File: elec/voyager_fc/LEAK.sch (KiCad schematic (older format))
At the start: 5 parts

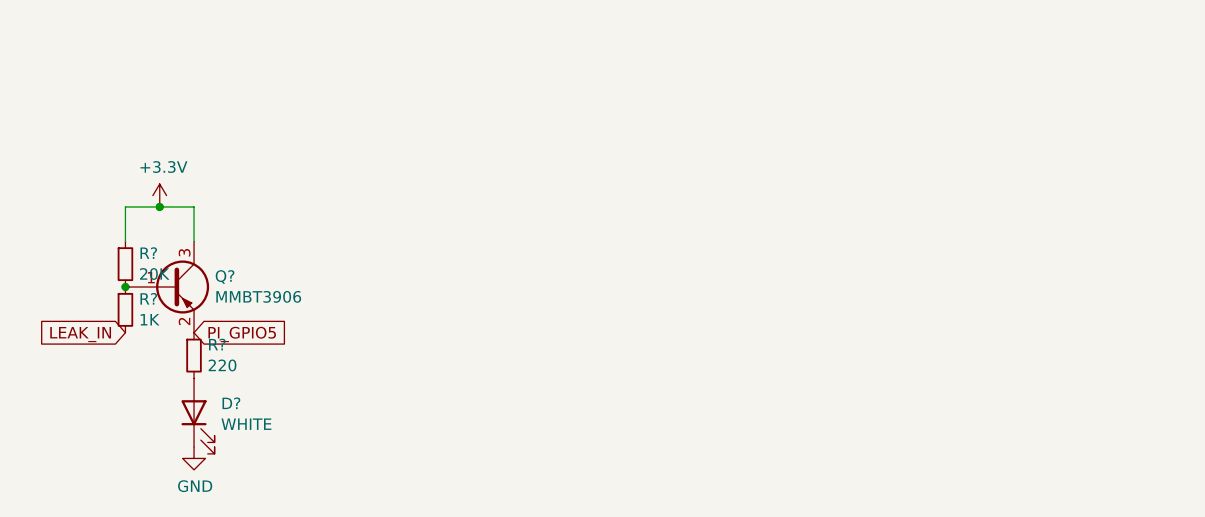
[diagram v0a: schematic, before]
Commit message: Move connectors inside schematics
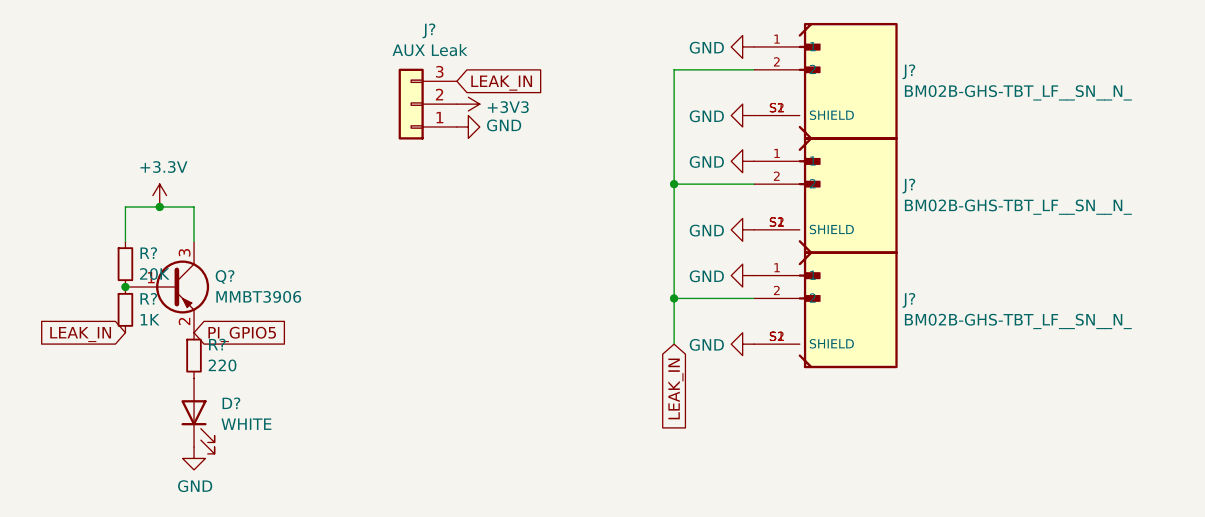
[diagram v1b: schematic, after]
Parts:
- added J? (x3): BM02B-GHS-TBT_LF__SN__N_, JST_BM02B-GHS-TBT_LF__SN__N_, symbol BM02B-GHS-TBT_LF__SN__N_:BM02B-GHS-TBT_LF__SN__N_
- added J?: AUX Leak, Connector_PinHeader_2.54mm:PinHeader_1x03_P2.54mm_Vertical, symbol Connector_Generic:Conn_01x03
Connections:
- net +3V3: now also J?.2 (Pin_2)
- net GND: now also J?.1, J?.1, J?.1, J?.1 (Pin_1), J?.S1 (SHIELD), J?.S1 (SHIELD), J?.S1 (SHIELD), J?.S2 (SHIELD), J?.S2 (SHIELD), J?.S2 (SHIELD)
- net LEAK_IN: now also J?.2, J?.2, J?.2, J?.3 (Pin_3)
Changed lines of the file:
@@
 $Descr A4 11693 8268
 encoding utf-8
-Sheet 6 9
+Sheet 5 9
 Title ""
 Date ""
@@
 U 1 1 67940941
 P 5300 4150
+AR Path="/67940941" Ref="#PWR?"  Part="1"
+AR Path="/6793F336/67940941" Ref="#PWR?"  Part="1"
 F 0 "#PWR?" H 5300 3900 50  0001 C CNN
 F 1 "GND" H 5305 3977 50  0000 C CNN
@@
 U 1 1 6794094C
 P 5150 3100
+AR Path="/6794094C" Ref="#PWR?"  Part="1"
+AR Path="/6793F336/6794094C" Ref="#PWR?"  Part="1"
 F 0 "#PWR?" H 5150 2950 50  0001 C CNN
 F 1 "+3.3V" H 5165 3273 50  0000 C CNN
@@
 U 1 1 67940952
 P 5300 4000
+AR Path="/67940952" Ref="D?"  Part="1"
+AR Path="/6793F336/67940952" Ref="D?"  Part="1"
 F 0 "D?" V 5339 3882 50  0000 R CNN
 F 1 "WHITE" V 5248 3882 50  0000 R CNN
@@
 U 1 1 67940958
 P 5300 3750
+AR Path="/67940958" Ref="R?"  Part="1"
+AR Path="/6793F336/67940958" Ref="R?"  Part="1"
 F 0 "R?" H 5359 3796 50  0000 L CNN
 F 1 "220" H 5359 3705 50  0000 L CNN
@@
 U 1 1 6794095E
 P 5000 3350
+AR Path="/6794095E" Ref="R?"  Part="1"
+AR Path="/6793F336/6794095E" Ref="R?"  Part="1"
 F 0 "R?" H 5059 3396 50  0000 L CNN
 F 1 "20K" H 5059 3305 50  0000 L CNN
@@
 U 1 1 67940965
 P 5000 3550
+AR Path="/67940965" Ref="R?"  Part="1"
+AR Path="/6793F336/67940965" Ref="R?"  Part="1"
 F 0 "R?" H 5059 3596 50  0000 L CNN
 F 1 "1K" H 5059 3505 50  0000 L CNN
@@
 U 1 1 6794096B
 P 5200 3450
+AR Path="/6794096B" Ref="Q?"  Part="1"
+AR Path="/6793F336/6794096B" Ref="Q?"  Part="1"
 F 0 "Q?" H 5391 3496 50  0000 L CNN
 F 1 "MMBT3906" H 5391 3405 50  0000 L CNN
@@
 	1    0    0    -1
 $EndComp
+$Comp
+L BM02B-GHS-TBT_LF__SN__N_:BM02B-GHS-TBT_LF__SN__N_ J?
+U 1 1 67D90B0B
+P 8150 3500
+F 0 "J?" H 8403 3496 50  0000 L CNN
+F 1 "BM02B-GHS-TBT_LF__SN__N_" H 8403 3405 50  0000 L CNN
+F 2 "JST_BM02B-GHS-TBT_LF__SN__N_" H 8150 3500 50  0001 L BNN
+F 3 "" H 8150 3500 50  0001 L BNN
+F 4 "JST Sales" H 8150 3500 50  0001 L BNN "MF"
+F 5 "4.05 mm" H 8150 3500 50  0001 L BNN "MAXIMUM_PACKAGE_HEIGHT"
+F 6 "None" H 8150 3500 50  0001 L BNN "Package"
+F 7 "None" H 8150 3500 50  0001 L BNN "Price"
+F 8 "https://www.snapeda.com/parts/BM02B-GHS-TBT(LF)(SN)(N)/JST+Sales+America+Inc./view-part/?ref=eda" H 8150 3500 50  0001 L BNN "Check_prices"
+F 9 "Manufacturer Recommendations" H 8150 3500 50  0001 L BNN "STANDARD"
+F 10 "https://www.snapeda.com/parts/BM02B-GHS-TBT(LF)(SN)(N)/JST+Sales+America+Inc./view-part/?ref=snap" H 8150 3500 50  0001 L BNN "SnapEDA_Link"
+F 11 "BM02B-GHS-TBT(LF)(SN)(N)" H 8150 3500 50  0001 L BNN "MP"
+F 12 "\\n                        \\n                            Connector Header Surface Mount 2 position 0.049 (1.25mm)\\n                        \\n" H 8150 3500 50  0001 L BNN "Description"
+F 13 "In Stock" H 8150 3500 50  0001 L BNN "Availability"
+F 14 "JST" H 8150 3500 50  0001 L BNN "MANUFACTURER"
+	1    8150 3500
+	1    0    0    -1
+$EndComp
+$Comp
+L BM02B-GHS-TBT_LF__SN__N_:BM02B-GHS-TBT_LF__SN__N_ J?
+U 1 1 67D90B1C
+P 8150 3000
+F 0 "J?" H 8403 2996 50  0000 L CNN
+F 1 "BM02B-GHS-TBT_LF__SN__N_" H 8403 2905 50  0000 L CNN
+F 2 "JST_BM02B-GHS-TBT_LF__SN__N_" H 8150 3000 50  0001 L BNN
+F 3 "" H 8150 3000 50  0001 L BNN
+F 4 "JST Sales" H 8150 3000 50  0001 L BNN "MF"
+F 5 "4.05 mm" H 8150 3000 50  0001 L BNN "MAXIMUM_PACKAGE_HEIGHT"
+F 6 "None" H 8150 3000 50  0001 L BNN "Package"
+F 7 "None" H 8150 3000 50  0001 L BNN "Price"
+F 8 "https://www.snapeda.com/parts/BM02B-GHS-TBT(LF)(SN)(N)/JST+Sales+America+Inc./view-part/?ref=eda" H 8150 3000 50  0001 L BNN "Check_prices"
+F 9 "Manufacturer Recommendations" H 8150 3000 50  0001 L BNN "STANDARD"
+F 10 "https://www.snapeda.com/parts/BM02B-GHS-TBT(LF)(SN)(N)/JST+Sales+America+Inc./view-part/?ref=snap" H 8150 3000 50  0001 L BNN "SnapEDA_Link"
+F 11 "BM02B-GHS-TBT(LF)(SN)(N)" H 8150 3000 50  0001 L BNN "MP"
+F 12 "\\n                        \\n                            Connector Header Surface Mount 2 position 0.049 (1.25mm)\\n                        \\n" H 8150 3000 50  0001 L BNN "Description"
+F 13 "In Stock" H 8150 3000 50  0001 L BNN "Availability"
+F 14 "JST" H 8150 3000 50  0001 L BNN "MANUFACTURER"
+	1    8150 3000
+	1    0    0    -1
+$EndComp
+$Comp
+L BM02B-GHS-TBT_LF__SN__N_:BM02B-GHS-TBT_LF__SN__N_ J?
+U 1 1 67D90B2D
+P 8150 2500
+F 0 "J?" H 8403 2496 50  0000 L CNN
+F 1 "BM02B-GHS-TBT_LF__SN__N_" H 8403 2405 50  0000 L CNN
+F 2 "JST_BM02B-GHS-TBT_LF__SN__N_" H 8150 2500 50  0001 L BNN
+F 3 "" H 8150 2500 50  0001 L BNN
+F 4 "JST Sales" H 8150 2500 50  0001 L BNN "MF"
+F 5 "4.05 mm" H 8150 2500 50  0001 L BNN "MAXIMUM_PACKAGE_HEIGHT"
+F 6 "None" H 8150 2500 50  0001 L BNN "Package"
+F 7 "None" H 8150 2500 50  0001 L BNN "Price"
+F 8 "https://www.snapeda.com/parts/BM02B-GHS-TBT(LF)(SN)(N)/JST+Sales+America+Inc./view-part/?ref=eda" H 8150 2500 50  0001 L BNN "Check_prices"
+F 9 "Manufacturer Recommendations" H 8150 2500 50  0001 L BNN "STANDARD"
+F 10 "https://www.snapeda.com/parts/BM02B-GHS-TBT(LF)(SN)(N)/JST+Sales+America+Inc./view-part/?ref=snap" H 8150 2500 50  0001 L BNN "SnapEDA_Link"
+F 11 "BM02B-GHS-TBT(LF)(SN)(N)" H 8150 2500 50  0001 L BNN "MP"
+F 12 "\\n                        \\n                            Connector Header Surface Mount 2 position 0.049 (1.25mm)\\n                        \\n" H 8150 2500 50  0001 L BNN "Description"
+F 13 "In Stock" H 8150 2500 50  0001 L BNN "Availability"
+F 14 "JST" H 8150 2500 50  0001 L BNN "MANUFACTURER"
+	1    8150 2500
+	1    0    0    -1
+$EndComp
+Wire Wire Line
+	7400 3000 7400 3500
+Connection ~ 7400 3000
+Wire Wire Line
+	7400 3500 7400 3700
+Connection ~ 7400 3500
+Wire Wire Line
+	7400 2500 7400 3000
+Wire Wire Line
+	7750 3500 7400 3500
+Wire Wire Line
+	7750 3000 7400 3000
+Wire Wire Line
+	7750 2500 7400 2500
+$Comp
+L power:GND #PWR?
+U 1 1 67D90B3B
+P 7750 2900
+F 0 "#PWR?" H 7750 2650 50  0001 C CNN
+F 1 "GND" V 7755 2772 50  0000 R CNN
+F 2 "" H 7750 2900 50  0001 C CNN
+F 3 "" H 7750 2900 50  0001 C CNN
+	1    7750 2900
+	0    1    1    0
+$EndComp
+$Comp
+L power:GND #PWR?
+U 1 1 67D90B41
+P 7750 2700
+F 0 "#PWR?" H 7750 2450 50  0001 C CNN
+F 1 "GND" V 7755 2572 50  0000 R CNN
+F 2 "" H 7750 2700 50  0001 C CNN
+F 3 "" H 7750 2700 50  0001 C CNN
+	1    7750 2700
+	0    1    1    0
+$EndComp
+$Comp
+L power:GND #PWR?
+U 1 1 67D90B47
+P 7750 3700
+F 0 "#PWR?" H 7750 3450 50  0001 C CNN
+F 1 "GND" V 7755 3572 50  0000 R CNN
+F 2 "" H 7750 3700 50  0001 C CNN
+F 3 "" H 7750 3700 50  0001 C CNN
+	1    7750 3700
+	0    1    1    0
+$EndComp
+$Comp
+L power:GND #PWR?
+U 1 1 67D90B4D
+P 7750 3400
+F 0 "#PWR?" H 7750 3150 50  0001 C CNN
+F 1 "GND" V 7755 3272 50  0000 R CNN
+F 2 "" H 7750 3400 50  0001 C CNN
+F 3 "" H 7750 3400 50  0001 C CNN
+	1    7750 3400
+	0    1    1    0
+$EndComp
+$Comp
+L power:GND #PWR?
+U 1 1 67D90B53
+P 7750 3200
+F 0 "#PWR?" H 7750 2950 50  0001 C CNN
+F 1 "GND" V 7755 3072 50  0000 R CNN
+F 2 "" H 7750 3200 50  0001 C CNN
+F 3 "" H 7750 3200 50  0001 C CNN
+	1    7750 3200
+	0    1    1    0
+$EndComp
+$Comp
+L power:GND #PWR?
+U 1 1 67D90B59
+P 7750 2400
+F 0 "#PWR?" H 7750 2150 50  0001 C CNN
+F 1 "GND" V 7755 2272 50  0000 R CNN
+F 2 "" H 7750 2400 50  0001 C CNN
+F 3 "" H 7750 2400 50  0001 C CNN
+	1    7750 2400
+	0    1    1    0
+$EndComp
+Text GLabel 7400 3700 3    50   Input ~ 0
+LEAK_IN
+$Comp
+L power:GND #PWR?
+U 1 1 67D90B60
+P 6450 2750
+F 0 "#PWR?" H 6450 2500 50  0001 C CNN
+F 1 "GND" V 6455 2622 50  0000 R CNN
+F 2 "" H 6450 2750 50  0001 C CNN
+F 3 "" H 6450 2750 50  0001 C CNN
+	1    6450 2750
+	0    -1   -1   0
+$EndComp
+Text GLabel 6450 2550 2    50   Input ~ 0
+LEAK_IN
+$Comp
+L power:+3V3 #PWR?
+U 1 1 67D90B67
+P 6450 2650
+F 0 "#PWR?" H 6450 2500 50  0001 C CNN
+F 1 "+3V3" V 6465 2778 50  0000 L CNN
+F 2 "" H 6450 2650 50  0001 C CNN
+F 3 "" H 6450 2650 50  0001 C CNN
+	1    6450 2650
+	0    1    1    0
+$EndComp
+$Comp
+L Connector_Generic:Conn_01x03 J?
+U 1 1 67D90B6D
+P 6250 2650
+F 0 "J?" H 6168 2325 50  0000 C CNN
+F 1 "AUX Leak" H 6168 2416 50  0000 C CNN
+F 2 "Connector_PinHeader_2.54mm:PinHeader_1x03_P2.54mm_Vertical" H 6250 2650 50  0001 C CNN
+F 3 "~" H 6250 2650 50  0001 C CNN
+	1    6250 2650
+	-1   0    0    1
+$EndComp
 $EndSCHEMATC

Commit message: Place all components and start route
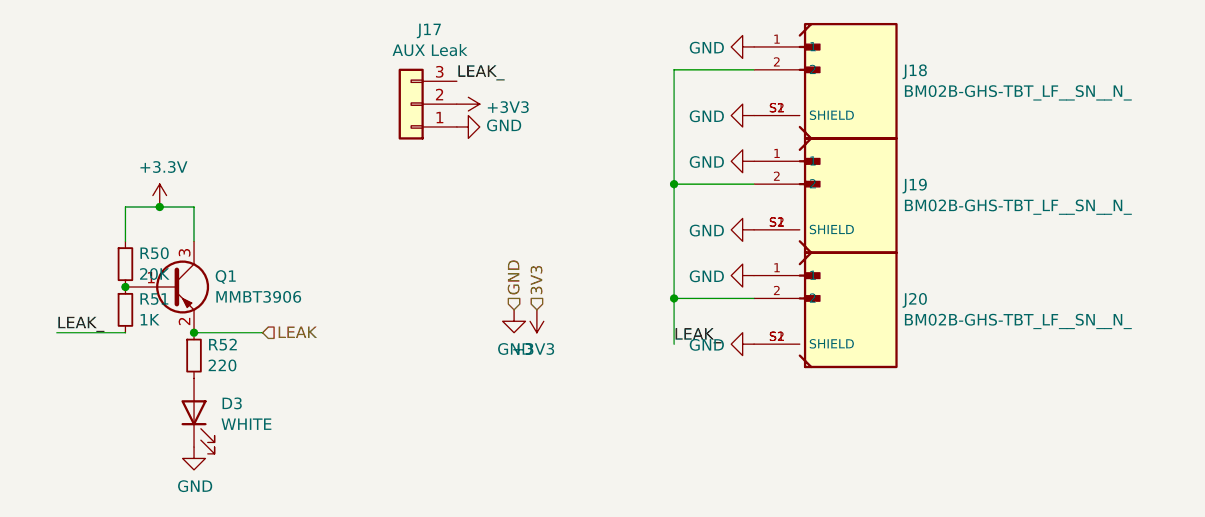
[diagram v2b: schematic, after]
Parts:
- J18, J19, J20: renamed from J?; footprint JST_BM02B-GHS-TBT_LF__SN__N_ -> BM02B-GHS-TBT_LF__SN__N_:JST_BM02B-GHS-TBT_LF__SN__N_
- R52: renamed from R?; footprint Resistor_SMD:R_0603_1608Metric -> Resistor_SMD:R_0402_1005Metric
- gave numbers to parts that had none: 5
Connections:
- net LEAK_IN renamed LEAK_
- net PI_GPIO5 renamed LEAK
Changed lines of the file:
@@
 $Descr A4 11693 8268
 encoding utf-8
-Sheet 5 9
+Sheet 5 10
 Title ""
 Date ""
@@
 Comment4 ""
 $EndDescr
-Text GLabel 5300 3650 2    50   Input ~ 0
-PI_GPIO5
-Text GLabel 5000 3650 0    50   Input ~ 0
-LEAK_IN
 $Comp
 L power:GND #PWR?
@@
 P 5300 4150
 AR Path="/67940941" Ref="#PWR?"  Part="1"
-AR Path="/6793F336/67940941" Ref="#PWR?"  Part="1"
-F 0 "#PWR?" H 5300 3900 50  0001 C CNN
+AR Path="/6793F336/67940941" Ref="#PWR0130"  Part="1"
+F 0 "#PWR0130" H 5300 3900 50  0001 C CNN
 F 1 "GND" H 5305 3977 50  0000 C CNN
 F 2 "" H 5300 4150 50  0001 C CNN
@@
 P 5150 3100
 AR Path="/6794094C" Ref="#PWR?"  Part="1"
-AR Path="/6793F336/6794094C" Ref="#PWR?"  Part="1"
-F 0 "#PWR?" H 5150 2950 50  0001 C CNN
+AR Path="/6793F336/6794094C" Ref="#PWR0129"  Part="1"
+F 0 "#PWR0129" H 5150 2950 50  0001 C CNN
 F 1 "+3.3V" H 5165 3273 50  0000 C CNN
 F 2 "" H 5150 3100 50  0001 C CNN
@@
 P 5300 4000
 AR Path="/67940952" Ref="D?"  Part="1"
-AR Path="/6793F336/67940952" Ref="D?"  Part="1"
-F 0 "D?" V 5339 3882 50  0000 R CNN
+AR Path="/6793F336/67940952" Ref="D3"  Part="1"
+F 0 "D3" V 5339 3882 50  0000 R CNN
 F 1 "WHITE" V 5248 3882 50  0000 R CNN
 F 2 "LED_SMD:LED_0603_1608Metric" H 5300 4000 50  0001 C CNN
@@
 P 5300 3750
 AR Path="/67940958" Ref="R?"  Part="1"
-AR Path="/6793F336/67940958" Ref="R?"  Part="1"
-F 0 "R?" H 5359 3796 50  0000 L CNN
+AR Path="/6793F336/67940958" Ref="R52"  Part="1"
+F 0 "R52" H 5359 3796 50  0000 L CNN
 F 1 "220" H 5359 3705 50  0000 L CNN
-F 2 "Resistor_SMD:R_0603_1608Metric" H 5300 3750 50  0001 C CNN
+F 2 "Resistor_SMD:R_0402_1005Metric" H 5300 3750 50  0001 C CNN
 F 3 "~" H 5300 3750 50  0001 C CNN
 	1    5300 3750
@@
 P 5000 3350
 AR Path="/6794095E" Ref="R?"  Part="1"
-AR Path="/6793F336/6794095E" Ref="R?"  Part="1"
-F 0 "R?" H 5059 3396 50  0000 L CNN
+AR Path="/6793F336/6794095E" Ref="R50"  Part="1"
+F 0 "R50" H 5059 3396 50  0000 L CNN
 F 1 "20K" H 5059 3305 50  0000 L CNN
 F 2 "Resistor_SMD:R_0603_1608Metric" H 5000 3350 50  0001 C CNN
@@
 P 5000 3550
 AR Path="/67940965" Ref="R?"  Part="1"
-AR Path="/6793F336/67940965" Ref="R?"  Part="1"
-F 0 "R?" H 5059 3596 50  0000 L CNN
+AR Path="/6793F336/67940965" Ref="R51"  Part="1"
+F 0 "R51" H 5059 3596 50  0000 L CNN
 F 1 "1K" H 5059 3505 50  0000 L CNN
 F 2 "Resistor_SMD:R_0603_1608Metric" H 5000 3550 50  0001 C CNN
@@
 P 5200 3450
 AR Path="/6794096B" Ref="Q?"  Part="1"
-AR Path="/6793F336/6794096B" Ref="Q?"  Part="1"
-F 0 "Q?" H 5391 3496 50  0000 L CNN
+AR Path="/6793F336/6794096B" Ref="Q1"  Part="1"
+F 0 "Q1" H 5391 3496 50  0000 L CNN
 F 1 "MMBT3906" H 5391 3405 50  0000 L CNN
 F 2 "Package_TO_SOT_SMD:SOT-23" H 5400 3375 50  0001 L CIN
@@
 U 1 1 67D90B0B
 P 8150 3500
-F 0 "J?" H 8403 3496 50  0000 L CNN
+AR Path="/67D90B0B" Ref="J?"  Part="1"
+AR Path="/6793F336/67D90B0B" Ref="J20"  Part="1"
+F 0 "J20" H 8403 3496 50  0000 L CNN
 F 1 "BM02B-GHS-TBT_LF__SN__N_" H 8403 3405 50  0000 L CNN
-F 2 "JST_BM02B-GHS-TBT_LF__SN__N_" H 8150 3500 50  0001 L BNN
+F 2 "BM02B-GHS-TBT_LF__SN__N_:JST_BM02B-GHS-TBT_LF__SN__N_" H 8150 3500 50  0001 L BNN
 F 3 "" H 8150 3500 50  0001 L BNN
 F 4 "JST Sales" H 8150 3500 50  0001 L BNN "MF"
@@
 U 1 1 67D90B1C
 P 8150 3000
-F 0 "J?" H 8403 2996 50  0000 L CNN
+AR Path="/67D90B1C" Ref="J?"  Part="1"
+AR Path="/6793F336/67D90B1C" Ref="J19"  Part="1"
+F 0 "J19" H 8403 2996 50  0000 L CNN
 F 1 "BM02B-GHS-TBT_LF__SN__N_" H 8403 2905 50  0000 L CNN
-F 2 "JST_BM02B-GHS-TBT_LF__SN__N_" H 8150 3000 50  0001 L BNN
+F 2 "BM02B-GHS-TBT_LF__SN__N_:JST_BM02B-GHS-TBT_LF__SN__N_" H 8150 3000 50  0001 L BNN
 F 3 "" H 8150 3000 50  0001 L BNN
 F 4 "JST Sales" H 8150 3000 50  0001 L BNN "MF"
@@
 U 1 1 67D90B2D
 P 8150 2500
-F 0 "J?" H 8403 2496 50  0000 L CNN
+AR Path="/67D90B2D" Ref="J?"  Part="1"
+AR Path="/6793F336/67D90B2D" Ref="J18"  Part="1"
+F 0 "J18" H 8403 2496 50  0000 L CNN
 F 1 "BM02B-GHS-TBT_LF__SN__N_" H 8403 2405 50  0000 L CNN
-F 2 "JST_BM02B-GHS-TBT_LF__SN__N_" H 8150 2500 50  0001 L BNN
+F 2 "BM02B-GHS-TBT_LF__SN__N_:JST_BM02B-GHS-TBT_LF__SN__N_" H 8150 2500 50  0001 L BNN
 F 3 "" H 8150 2500 50  0001 L BNN
 F 4 "JST Sales" H 8150 2500 50  0001 L BNN "MF"
@@
 U 1 1 67D90B3B
 P 7750 2900
-F 0 "#PWR?" H 7750 2650 50  0001 C CNN
+AR Path="/67D90B3B" Ref="#PWR?"  Part="1"
+AR Path="/6793F336/67D90B3B" Ref="#PWR0137"  Part="1"
+F 0 "#PWR0137" H 7750 2650 50  0001 C CNN
 F 1 "GND" V 7755 2772 50  0000 R CNN
 F 2 "" H 7750 2900 50  0001 C CNN
@@
 U 1 1 67D90B41
 P 7750 2700
-F 0 "#PWR?" H 7750 2450 50  0001 C CNN
+AR Path="/67D90B41" Ref="#PWR?"  Part="1"
+AR Path="/6793F336/67D90B41" Ref="#PWR0136"  Part="1"
+F 0 "#PWR0136" H 7750 2450 50  0001 C CNN
 F 1 "GND" V 7755 2572 50  0000 R CNN
 F 2 "" H 7750 2700 50  0001 C CNN
@@
 U 1 1 67D90B47
 P 7750 3700
-F 0 "#PWR?" H 7750 3450 50  0001 C CNN
+AR Path="/67D90B47" Ref="#PWR?"  Part="1"
+AR Path="/6793F336/67D90B47" Ref="#PWR0140"  Part="1"
+F 0 "#PWR0140" H 7750 3450 50  0001 C CNN
 F 1 "GND" V 7755 3572 50  0000 R CNN
 F 2 "" H 7750 3700 50  0001 C CNN
@@
 U 1 1 67D90B4D
 P 7750 3400
-F 0 "#PWR?" H 7750 3150 50  0001 C CNN
+AR Path="/67D90B4D" Ref="#PWR?"  Part="1"
+AR Path="/6793F336/67D90B4D" Ref="#PWR0139"  Part="1"
+F 0 "#PWR0139" H 7750 3150 50  0001 C CNN
 F 1 "GND" V 7755 3272 50  0000 R CNN
 F 2 "" H 7750 3400 50  0001 C CNN
@@
 U 1 1 67D90B53
 P 7750 3200
-F 0 "#PWR?" H 7750 2950 50  0001 C CNN
+AR Path="/67D90B53" Ref="#PWR?"  Part="1"
+AR Path="/6793F336/67D90B53" Ref="#PWR0138"  Part="1"
+F 0 "#PWR0138" H 7750 2950 50  0001 C CNN
 F 1 "GND" V 7755 3072 50  0000 R CNN
 F 2 "" H 7750 3200 50  0001 C CNN
@@
 U 1 1 67D90B59
 P 7750 2400
-F 0 "#PWR?" H 7750 2150 50  0001 C CNN
+AR Path="/67D90B59" Ref="#PWR?"  Part="1"
+AR Path="/6793F336/67D90B59" Ref="#PWR0135"  Part="1"
+F 0 "#PWR0135" H 7750 2150 50  0001 C CNN
 F 1 "GND" V 7755 2272 50  0000 R CNN
 F 2 "" H 7750 2400 50  0001 C CNN
@@
 	0    1    1    0
 $EndComp
-Text GLabel 7400 3700 3    50   Input ~ 0
-LEAK_IN
 $Comp
 L power:GND #PWR?
 U 1 1 67D90B60
 P 6450 2750
-F 0 "#PWR?" H 6450 2500 50  0001 C CNN
+AR Path="/67D90B60" Ref="#PWR?"  Part="1"
+AR Path="/6793F336/67D90B60" Ref="#PWR0132"  Part="1"
+F 0 "#PWR0132" H 6450 2500 50  0001 C CNN
 F 1 "GND" V 6455 2622 50  0000 R CNN
 F 2 "" H 6450 2750 50  0001 C CNN
@@
 	0    -1   -1   0
 $EndComp
-Text GLabel 6450 2550 2    50   Input ~ 0
-LEAK_IN
 $Comp
 L power:+3V3 #PWR?
 U 1 1 67D90B67
 P 6450 2650
-F 0 "#PWR?" H 6450 2500 50  0001 C CNN
+AR Path="/67D90B67" Ref="#PWR?"  Part="1"
+AR Path="/6793F336/67D90B67" Ref="#PWR0131"  Part="1"
+F 0 "#PWR0131" H 6450 2500 50  0001 C CNN
 F 1 "+3V3" V 6465 2778 50  0000 L CNN
 F 2 "" H 6450 2650 50  0001 C CNN
@@
 U 1 1 67D90B6D
 P 6250 2650
-F 0 "J?" H 6168 2325 50  0000 C CNN
+AR Path="/67D90B6D" Ref="J?"  Part="1"
+AR Path="/6793F336/67D90B6D" Ref="J17"  Part="1"
+F 0 "J17" H 6168 2325 50  0000 C CNN
 F 1 "AUX Leak" H 6168 2416 50  0000 C CNN
 F 2 "Connector_PinHeader_2.54mm:PinHeader_1x03_P2.54mm_Vertical" H 6250 2650 50  0001 C CNN
@@
 	-1   0    0    1
 $EndComp
+Wire Wire Line
+	5300 3650 5600 3650
+Connection ~ 5300 3650
+Text HLabel 5600 3650 2    50   Input ~ 0
+LEAK
+Wire Wire Line
+	5000 3650 4700 3650
+Text Label 4700 3650 0    50   ~ 0
+LEAK_
+Text Label 6450 2550 0    50   ~ 0
+LEAK_
+Text Label 7400 3700 0    50   ~ 0
+LEAK_
+Text HLabel 6800 3550 1    50   Input ~ 0
+3V3
+$Comp
+L power:+3V3 #PWR0134
+U 1 1 672DE5BA
+P 6800 3550
+F 0 "#PWR0134" H 6800 3400 50  0001 C CNN
+F 1 "+3V3" H 6815 3723 50  0000 C CNN
+F 2 "" H 6800 3550 50  0001 C CNN
+F 3 "" H 6800 3550 50  0001 C CNN
+	1    6800 3550
+	-1   0    0    1
+$EndComp
+Text HLabel 6700 3550 1    50   Input ~ 0
+GND
+$Comp
+L power:GND #PWR0133
+U 1 1 672E022C
+P 6700 3550
+F 0 "#PWR0133" H 6700 3300 50  0001 C CNN
+F 1 "GND" H 6705 3377 50  0000 C CNN
+F 2 "" H 6700 3550 50  0001 C CNN
+F 3 "" H 6700 3550 50  0001 C CNN
+	1    6700 3550
+	1    0    0    -1
+$EndComp
 $EndSCHEMATC
